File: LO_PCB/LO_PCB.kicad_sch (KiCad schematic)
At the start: 98 parts, among them J1 PWR, J2 Conn_01x06, Q1 AO3401A, U1 TPS7A9101DSKT, U2 LMX2582RHAR, X1 TB612-100.0M

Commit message: updated component values yet again and concluded a need an adapter board if i want to reuse the on board reference for other stuff
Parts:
- C46: Dielectric (none) -> C0G/NP0; MPN (none) -> GRM1555C1H150JA01D; Manufacturer (none) -> Murata; Tolerance (none) -> +/-5%; Voltage (none) -> 50V
- R23: value 47 -> 62; MPN RG1005P-470-B-T5 -> RG1005P-620-B-T5
- R24: value 18 -> 68; MPN RC0402FR-0718RL -> RC0402FR-0768RL
- R25, R27: value 18 -> 0; MPN RC0402FR-0718RL -> RC0402JR-070RL; Tolerance +/-1% -> jumper, <0.05R
- R29: value 56 -> 82; MPN RG1005P-560-B-T5 -> RG1005P-820-B-T5
- R30: value 36 -> 49.9; MPN ESR01MZPF36R0 -> RG1005P-49R9-B-T5; Manufacturer Rohm -> Susumu; Tolerance +/-1% -> +/-0.1%
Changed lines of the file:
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@@
 			)
 		)
-		(property "MPN" ""
+		(property "MPN" "GRM1555C1H150JA01D"
 			(at 109.22 193.04 0)
 			(hide yes)
@@
 			)
 		)
-		(property "Manufacturer" ""
+		(property "Manufacturer" "Murata"
 			(at 109.22 193.04 0)
 			(hide yes)
@@
 			)
 		)
-		(property "Dielectric" ""
+		(property "Dielectric" "C0G/NP0"
 			(at 109.22 193.04 0)
 			(hide yes)
@@
 			)
 		)
-		(property "Voltage" ""
+		(property "Voltage" "50V"
 			(at 109.22 193.04 0)
 			(hide yes)
@@
 			)
 		)
-		(property "Tolerance" ""
+		(property "Tolerance" "+/-5%"
 			(at 109.22 193.04 0)
 			(hide yes)
@@
 			)
 		)
-		(property "Value" "36"
+		(property "Value" "49.9"
 			(at 108.204 228.6 0)
 			(show_name no)
@@
 			)
 		)
-		(property "MPN" "ESR01MZPF36R0"
+		(property "MPN" "RG1005P-49R9-B-T5"
 			(at 106.68 227.33 0)
 			(hide yes)
@@
 			)
 		)
-		(property "Manufacturer" "Rohm"
+		(property "Manufacturer" "Susumu"
 			(at 106.68 227.33 0)
 			(hide yes)
@@
 			)
 		)
-		(property "Tolerance" "+/-1%"
+		(property "Tolerance" "+/-0.1%"
 			(at 106.68 227.33 0)
 			(hide yes)
@@
 			)
 		)
-		(property "Value" "56"
+		(property "Value" "82"
 			(at 99.314 228.6 0)
 			(show_name no)
@@
 			)
 		)
-		(property "MPN" "RG1005P-560-B-T5"
+		(property "MPN" "RG1005P-820-B-T5"
 			(at 97.79 227.33 0)
 			(hide yes)
@@
 			)
 		)
-		(property "Value" "18"
+		(property "Value" "68"
 			(at 91.44 213.36 90)
 			(show_name no)
@@
 			)
 		)
-		(property "MPN" "RC0402FR-0718RL"
+		(property "MPN" "RC0402FR-0768RL"
 			(at 90.17 210.82 0)
 			(hide yes)
@@
 			)
 		)
-		(property "Value" "47"
+		(property "Value" "62"
 			(at 99.314 204.47 0)
 			(show_name no)
@@
 			)
 		)
-		(property "MPN" "RG1005P-470-B-T5"
+		(property "MPN" "RG1005P-620-B-T5"
 			(at 97.79 203.2 0)
 			(hide yes)
@@
 			)
 		)
-		(property "Value" "18"
+		(property "Value" "0"
 			(at 115.57 213.36 90)
 			(show_name no)
@@
 			)
 		)
-		(property "MPN" "RC0402FR-0718RL"
+		(property "MPN" "RC0402JR-070RL"
 			(at 114.3 210.82 0)
 			(hide yes)
@@
 			)
 		)
-		(property "Tolerance" "+/-1%"
+		(property "Tolerance" "jumper, <0.05R"
 			(at 114.3 210.82 0)
 			(hide yes)
@@
 			)
 		)
-		(property "Value" "18"
+		(property "Value" "0"
 			(at 115.57 222.25 90)
 			(show_name no)
@@
 			)
 		)
-		(property "MPN" "RC0402FR-0718RL"
+		(property "MPN" "RC0402JR-070RL"
 			(at 114.3 219.71 0)
 			(hide yes)
@@
 			)
 		)
-		(property "Tolerance" "+/-1%"
+		(property "Tolerance" "jumper, <0.05R"
 			(at 114.3 219.71 0)
 			(hide yes)

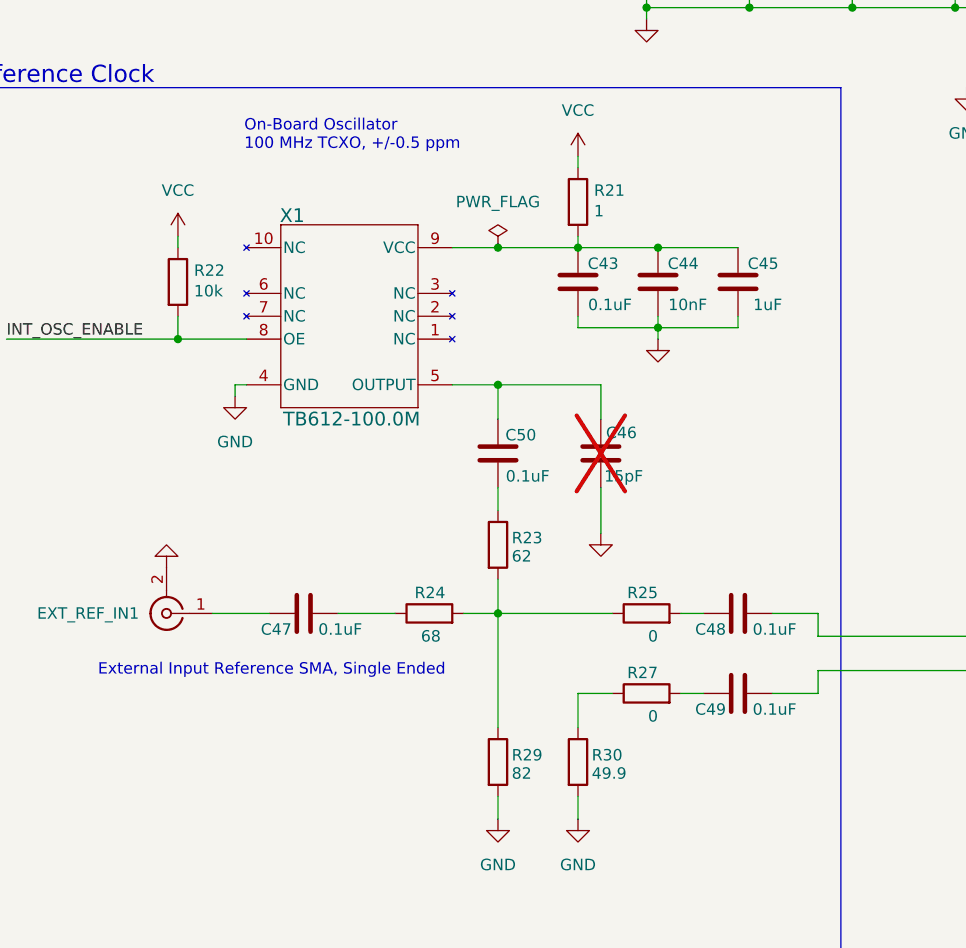
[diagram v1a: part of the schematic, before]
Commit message: updated the LO schematic to better match the external reference usecase
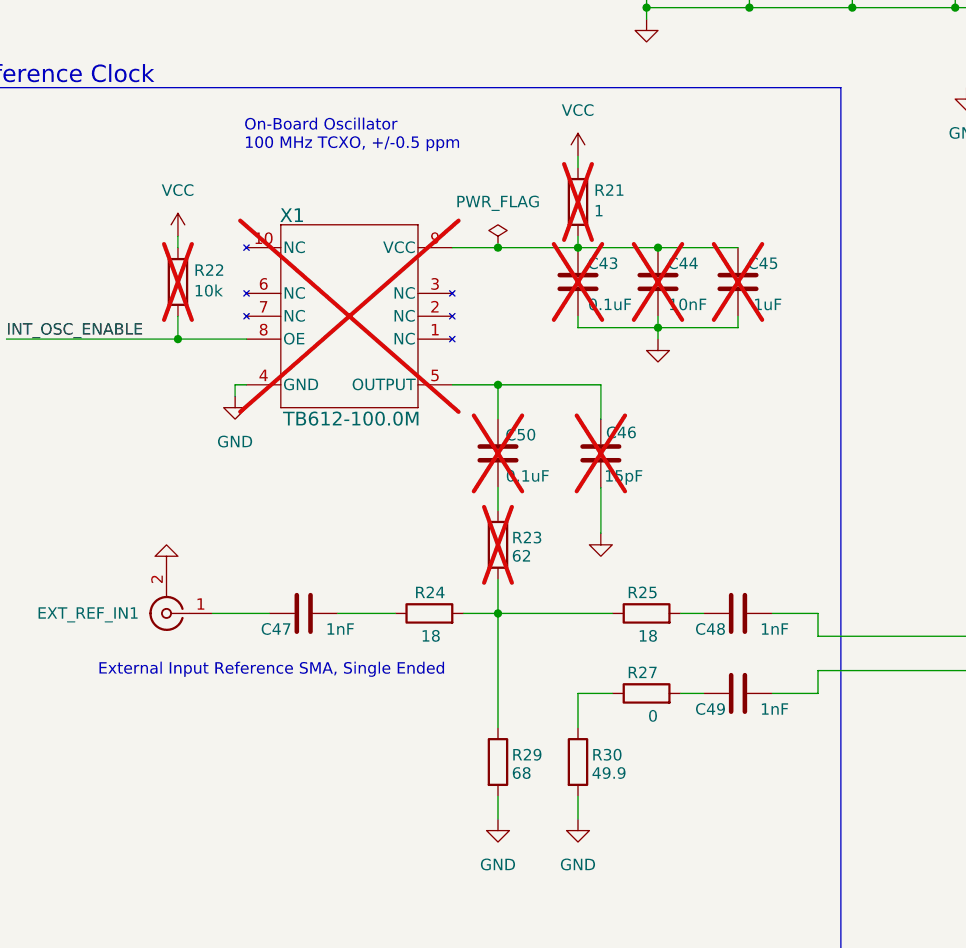
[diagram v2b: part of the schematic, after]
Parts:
- C43, C44, C45, C50, R21, R22, R23, X1: now not fitted
- C47, C48, C49: value 0.1uF -> 1nF; Dielectric X7R -> C0G/NP0; MPN GRM155R71H104KE14D -> GRM1555C1H102JA01D; Tolerance +/-10% -> +/-5%; Voltage 25V -> 50V
- R24: value 68 -> 18; MPN RC0402FR-0768RL -> RC0402FR-0718RL
- R25: value 0 -> 18; MPN RC0402JR-070RL -> RC0402FR-0718RL; Tolerance jumper, <0.05R -> +/-1%
- R29: value 82 -> 68; MPN RG1005P-820-B-T5 -> RC0402FR-0768RL; Manufacturer Susumu -> Yageo; Tolerance +/-0.1% -> +/-1%
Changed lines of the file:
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@@
 			)
 		)
-		(property "Value" "0.1uF"
+		(property "Value" "1nF"
 			(at 128.524 212.598 90)
 			(show_name no)
@@
 			)
 		)
-		(property "MPN" "GRM155R71H104KE14D"
+		(property "MPN" "GRM1555C1H102JA01D"
 			(at 124.46 210.82 0)
 			(hide yes)
@@
 			)
 		)
-		(property "Dielectric" "X7R"
+		(property "Dielectric" "C0G/NP0"
 			(at 124.46 210.82 0)
 			(hide yes)
@@
 			)
 		)
-		(property "Voltage" "25V"
+		(property "Voltage" "50V"
 			(at 124.46 210.82 0)
 			(hide yes)
@@
 			)
 		)
-		(property "Tolerance" "+/-10%"
+		(property "Tolerance" "+/-5%"
 			(at 124.46 210.82 0)
 			(hide yes)
@@
 			)
 		)
-		(property "Value" "0.1uF"
+		(property "Value" "1nF"
 			(at 128.524 221.488 90)
 			(show_name no)
@@
 			)
 		)
-		(property "MPN" "GRM155R71H104KE14D"
+		(property "MPN" "GRM1555C1H102JA01D"
 			(at 124.46 219.71 0)
 			(hide yes)
@@
 			)
 		)
-		(property "Dielectric" "X7R"
+		(property "Dielectric" "C0G/NP0"
 			(at 124.46 219.71 0)
 			(hide yes)
@@
 			)
 		)
-		(property "Voltage" "25V"
+		(property "Voltage" "50V"
 			(at 124.46 219.71 0)
 			(hide yes)
@@
 			)
 		)
-		(property "Tolerance" "+/-10%"
+		(property "Tolerance" "+/-5%"
 			(at 124.46 219.71 0)
 			(hide yes)
@@
 		(on_board yes)
 		(in_pos_files yes)
-		(dnp no)
+		(dnp yes)
 		(property "Reference" "R21"
 			(at 108.458 163.83 0)
@@
 			)
 		)
-		(property "Value" "82"
+		(property "Value" "68"
 			(at 99.314 228.6 0)
 			(show_name no)
@@
 			)
 		)
-		(property "MPN" "RG1005P-820-B-T5"
+		(property "MPN" "RC0402FR-0768RL"
 			(at 97.79 227.33 0)
 			(hide yes)
@@
 			)
 		)
-		(property "Manufacturer" "Susumu"
+		(property "Manufacturer" "Yageo"
 			(at 97.79 227.33 0)
 			(hide yes)
@@
 			)
 		)
-		(property "Tolerance" "+/-0.1%"
+		(property "Tolerance" "+/-1%"
 			(at 97.79 227.33 0)
 			(hide yes)
@@
 		(on_board yes)
 		(in_pos_files yes)
-		(dnp no)
+		(dnp yes)
 		(property "Reference" "C45"
 			(at 127.254 171.958 0)
@@
 		(on_board yes)
 		(in_pos_files yes)
-		(dnp no)
+		(dnp yes)
 		(property "Reference" "C43"
 			(at 109.474 171.958 0)
@@
 			)
 		)
-		(property "Value" "0.1uF"
+		(property "Value" "1nF"
 			(at 80.264 212.598 90)
 			(show_name no)
@@
 			)
 		)
-		(property "MPN" "GRM155R71H104KE14D"
+		(property "MPN" "GRM1555C1H102JA01D"
 			(at 76.2 210.82 0)
 			(hide yes)
@@
 			)
 		)
-		(property "Dielectric" "X7R"
+		(property "Dielectric" "C0G/NP0"
 			(at 76.2 210.82 0)
 			(hide yes)
@@
 			)
 		)
-		(property "Voltage" "25V"
+		(property "Voltage" "50V"
 			(at 76.2 210.82 0)
 			(hide yes)
@@
 			)
 		)
-		(property "Tolerance" "+/-10%"
+		(property "Tolerance" "+/-5%"
 			(at 76.2 210.82 0)
 			(hide yes)
@@
 			)
 		)
-		(property "Value" "68"
+		(property "Value" "18"
 			(at 91.44 213.36 90)
 			(show_name no)
@@
 			)
 		)
-		(property "MPN" "RC0402FR-0768RL"
+		(property "MPN" "RC0402FR-0718RL"
 			(at 90.17 210.82 0)
 			(hide yes)
@@
 		(on_board yes)
 		(in_pos_files yes)
-		(dnp no)
+		(dnp yes)
 		(property "Reference" "X1"
 			(at 74.93 166.624 0)
@@
 		(on_board yes)
 		(in_pos_files yes)
-		(dnp no)
+		(dnp yes)
 		(property "Reference" "R22"
 			(at 64.008 172.72 0)
@@
 		(on_board yes)
 		(in_pos_files yes)
-		(dnp no)
+		(dnp yes)
 		(property "Reference" "R23"
 			(at 99.314 202.438 0)
@@
 		(on_board yes)
 		(in_pos_files yes)
-		(dnp no)
+		(dnp yes)
 		(property "Reference" "C44"
 			(at 118.364 171.958 0)
@@
 		(on_board yes)
 		(in_pos_files yes)
-		(dnp no)
+		(dnp yes)
 		(property "Reference" "C50"
 			(at 100.33 191.008 0)
@@
 			)
 		)
-		(property "Value" "0"
+		(property "Value" "18"
 			(at 115.57 213.36 90)
 			(show_name no)
@@
 			)
 		)
-		(property "MPN" "RC0402JR-070RL"
+		(property "MPN" "RC0402FR-0718RL"
 			(at 114.3 210.82 0)
 			(hide yes)
@@
 			)
 		)
-		(property "Tolerance" "jumper, <0.05R"
+		(property "Tolerance" "+/-1%"
 			(at 114.3 210.82 0)
 			(hide yes)

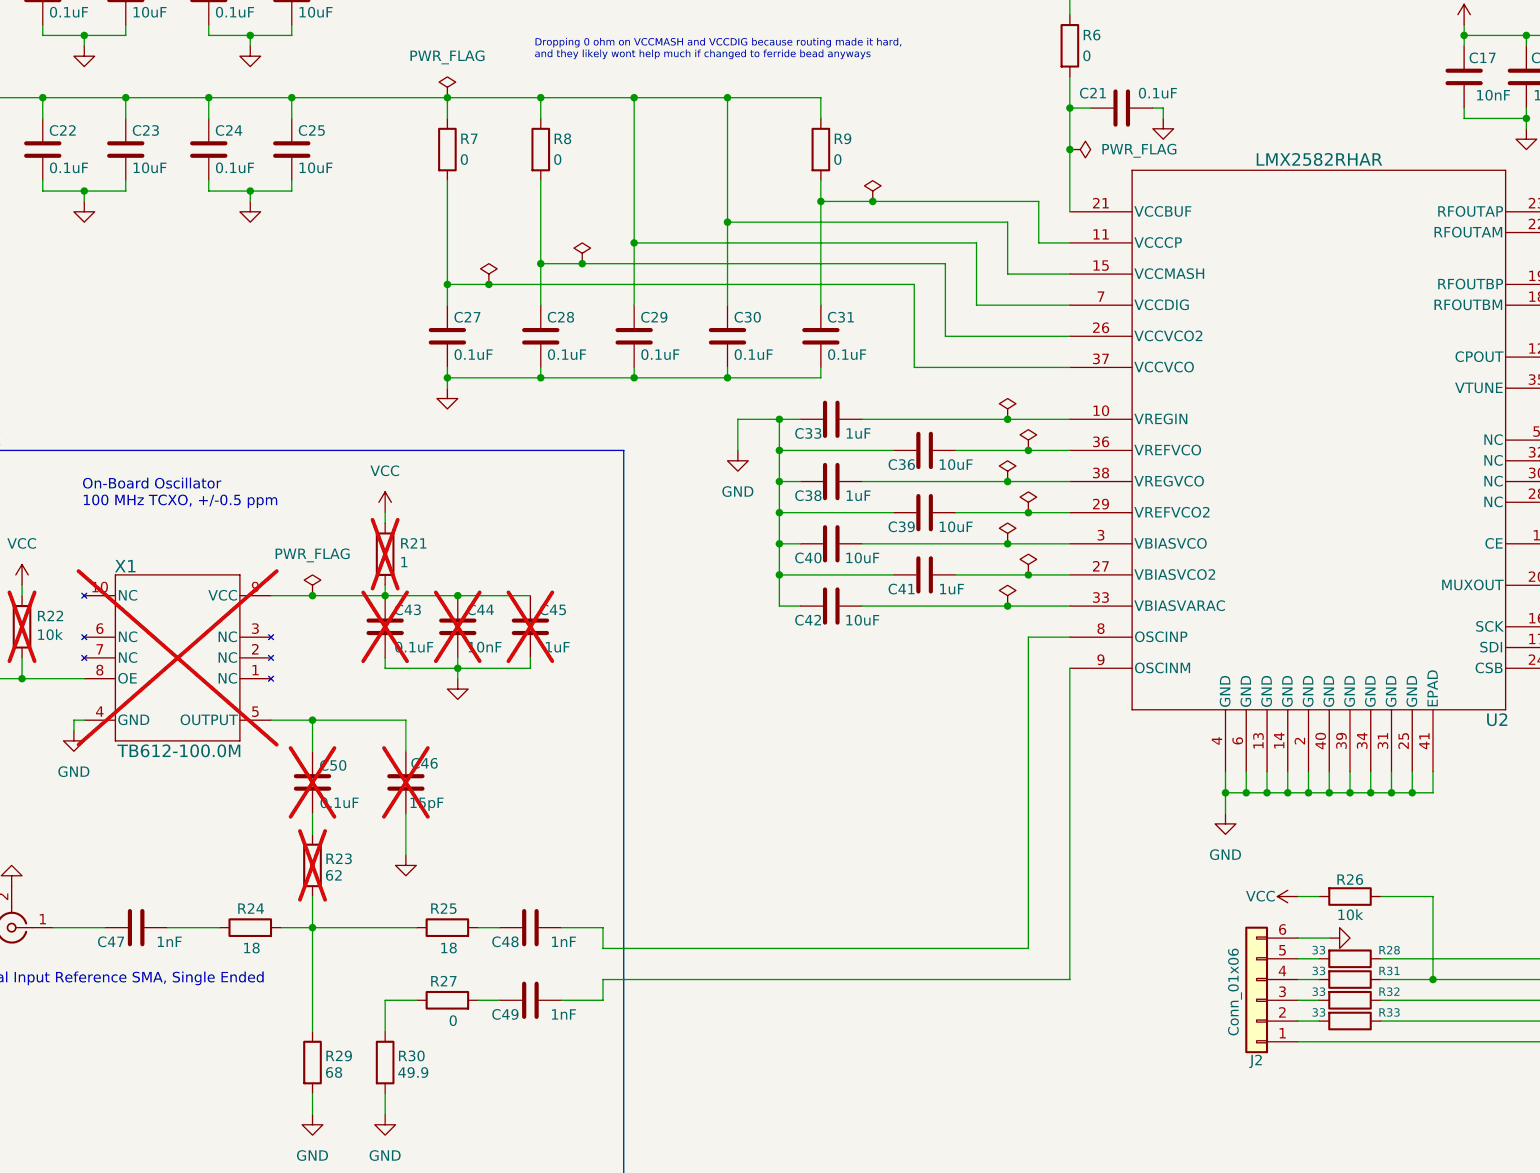
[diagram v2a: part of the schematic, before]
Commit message: updated the symbol in LO board from lmx2582 to lmx2592 in order to cover the upper range of the 5Ghz spectrum. drop in replacement
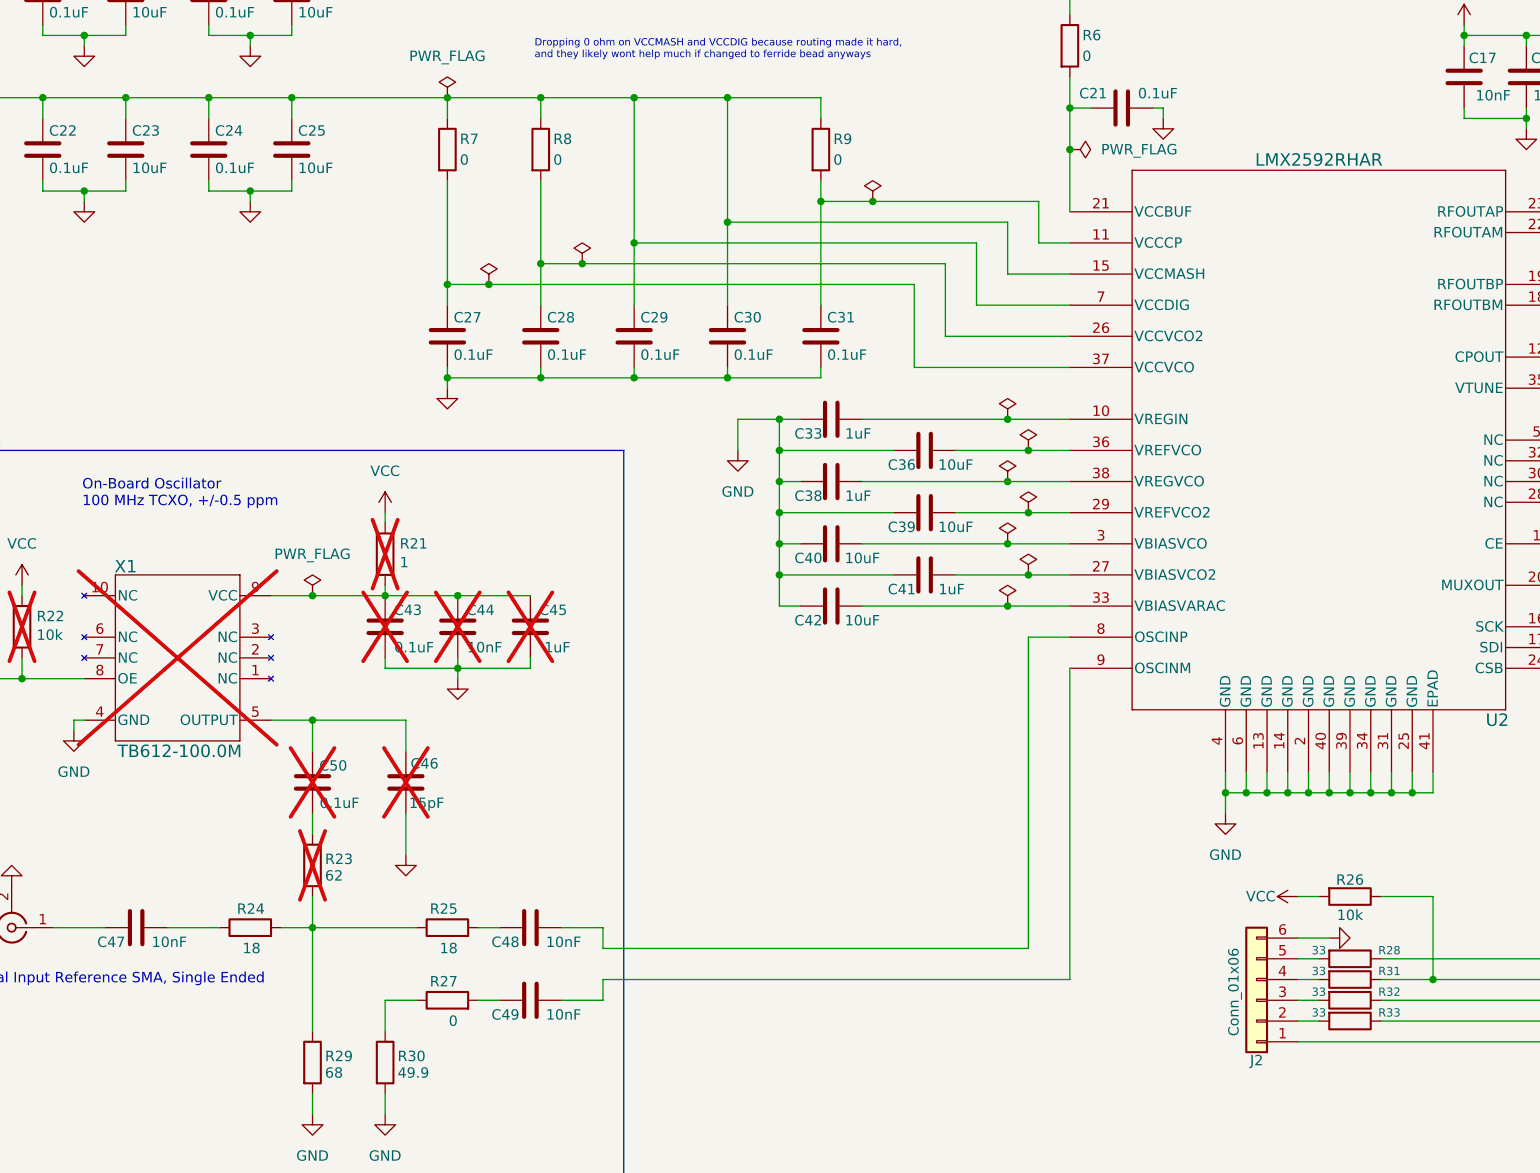
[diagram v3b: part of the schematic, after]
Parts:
- C47, C48, C49: value 1nF -> 10nF; Dielectric C0G/NP0 -> X7R; MPN GRM1555C1H102JA01D -> GRM155R71H103KA88D; Tolerance +/-5% -> +/-10%
- U2: value LMX2582RHAR -> LMX2592RHAR; symbol Snapeda:LMX2582RHAR -> Snapeda:LMX2592RHAR; MPN LMX2582RHAR -> LMX2592RHAR
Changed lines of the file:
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@@
 			)
 		)
-		(property "Value" "1nF"
+		(property "Value" "10nF"
 			(at 128.524 212.598 90)
 			(show_name no)
@@
 			)
 		)
-		(property "MPN" "GRM1555C1H102JA01D"
+		(property "MPN" "GRM155R71H103KA88D"
 			(at 124.46 210.82 0)
 			(hide yes)
@@
 			)
 		)
-		(property "Dielectric" "C0G/NP0"
+		(property "Dielectric" "X7R"
 			(at 124.46 210.82 0)
 			(hide yes)
@@
 			)
 		)
-		(property "Tolerance" "+/-5%"
+		(property "Tolerance" "+/-10%"
 			(at 124.46 210.82 0)
 			(hide yes)
@@
 			)
 		)
-		(property "Value" "1nF"
+		(property "Value" "10nF"
 			(at 128.524 221.488 90)
 			(show_name no)
@@
 			)
 		)
-		(property "MPN" "GRM1555C1H102JA01D"
+		(property "MPN" "GRM155R71H103KA88D"
 			(at 124.46 219.71 0)
 			(hide yes)
@@
 			)
 		)
-		(property "Dielectric" "C0G/NP0"
+		(property "Dielectric" "X7R"
 			(at 124.46 219.71 0)
 			(hide yes)
@@
 			)
 		)
-		(property "Tolerance" "+/-5%"
+		(property "Tolerance" "+/-10%"
 			(at 124.46 219.71 0)
 			(hide yes)
@@
 			)
 		)
-		(property "Value" "1nF"
+		(property "Value" "10nF"
 			(at 80.264 212.598 90)
 			(show_name no)
@@
 			)
 		)
-		(property "MPN" "GRM1555C1H102JA01D"
+		(property "MPN" "GRM155R71H103KA88D"
 			(at 76.2 210.82 0)
 			(hide yes)
@@
 			)
 		)
-		(property "Dielectric" "C0G/NP0"
+		(property "Dielectric" "X7R"
 			(at 76.2 210.82 0)
 			(hide yes)
@@
 			)
 		)
-		(property "Tolerance" "+/-5%"
+		(property "Tolerance" "+/-10%"
 			(at 76.2 210.82 0)
 			(hide yes)
@@
 	)
 	(symbol
-		(lib_id "Snapeda:LMX2582RHAR")
+		(lib_id "Snapeda:LMX2592RHAR")
 		(at 190.5 123.19 0)
 		(unit 1)
@@
 			)
 		)
-		(property "Value" "LMX2582RHAR"
+		(property "Value" "LMX2592RHAR"
 			(at 220.98 116.84 0)
 			(show_name no)
@@
 			)
 		)
-		(property "Datasheet" "https://www.ti.com/lit/gpn/lmx2582"
+		(property "Datasheet" "https://www.ti.com/lit/gpn/lmx2592"
 			(at 220.98 115.57 0)
 			(hide yes)
@@
 			)
 		)
-		(property "MPN" "LMX2582RHAR"
+		(property "MPN" "LMX2592RHAR"
 			(at 190.5 123.19 0)
 			(hide yes)
